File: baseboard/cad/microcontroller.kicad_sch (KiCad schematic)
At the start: 12 parts, among them J16 Conn_01x04_Pin, K1 TQ2-L2-3V3, K2 TQ2-L2-3V3, SW3 SW_DIP_x01, U10 STM32L011F3Ux, U11 DRV8212P, U12 DRV8212P, Y1 830054236

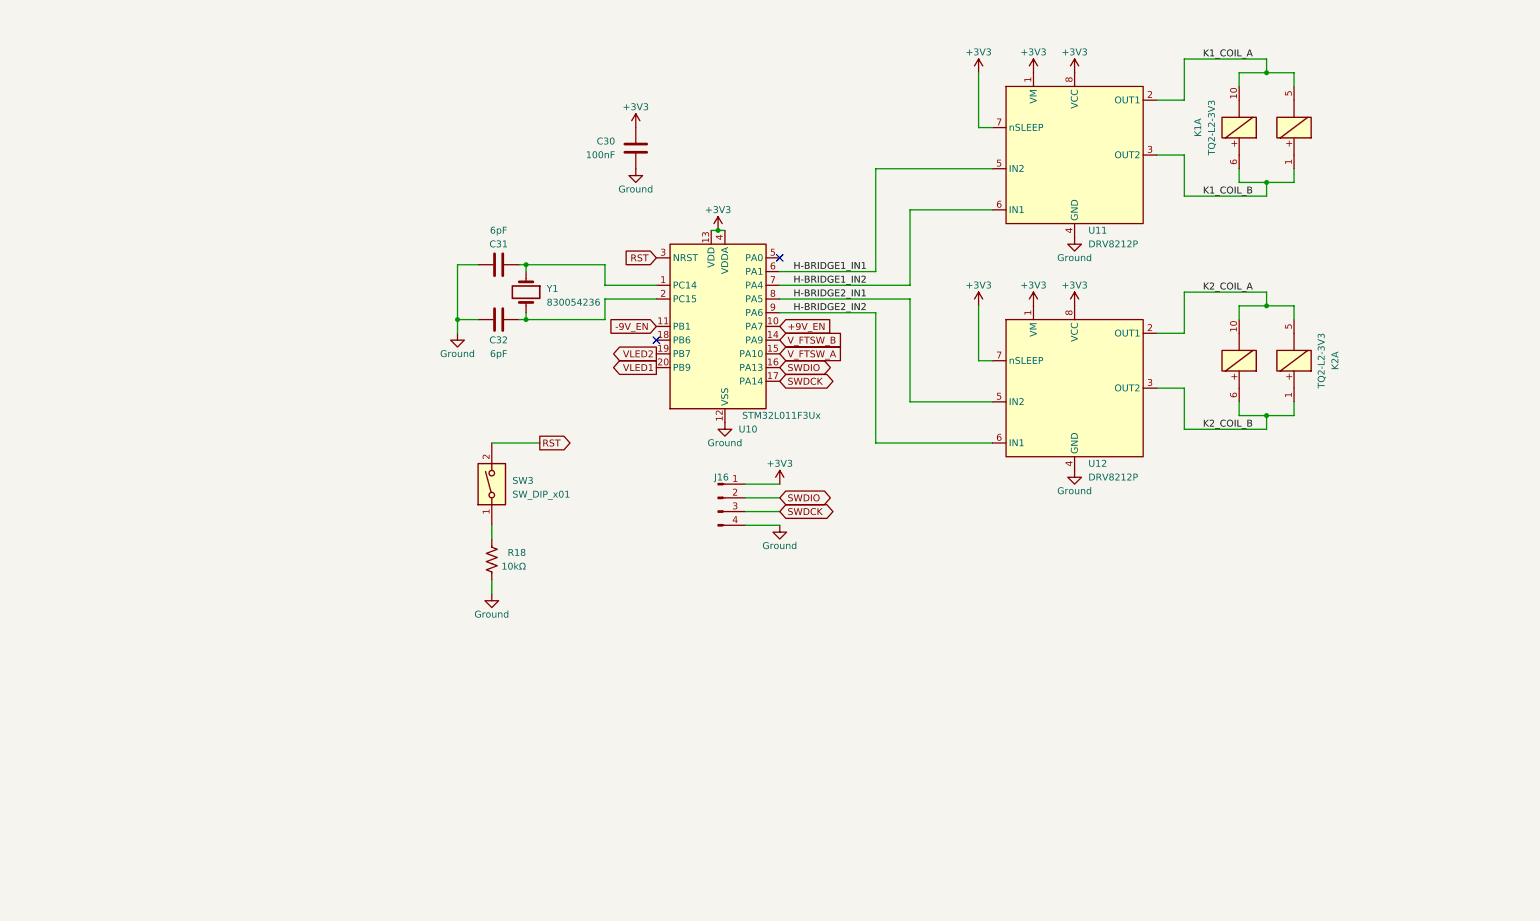
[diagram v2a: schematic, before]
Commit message: swapped micro and started layout
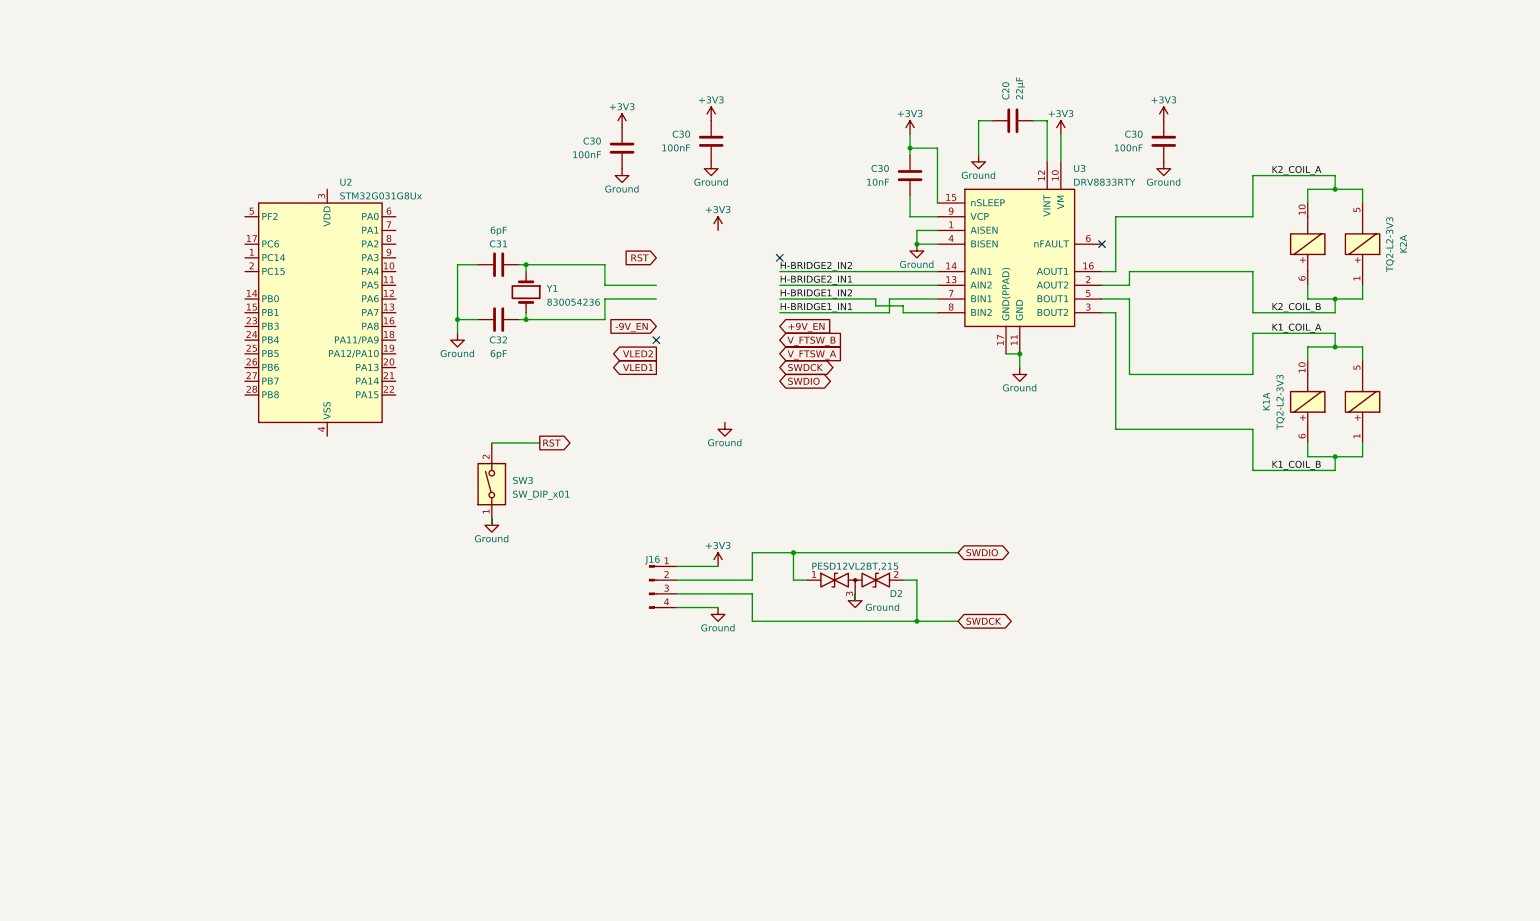
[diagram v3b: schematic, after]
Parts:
- removed R18: 10kΩ, Resistor_SMD:R_0603_1608Metric, symbol Device:R_US
- removed U10: STM32L011F3Ux, Package_DFN_QFN:ST_UFQFPN-20_3x3mm_P0.5mm, symbol MCU_ST_STM32L0:STM32L011F3Ux
- removed U11, U12: DRV8212P, Package_SON:WSON-8-1EP_2x2mm_P0.5mm_EP0.9x1.6mm, symbol Library:DRV8212P
- added C20: 22μF, Capacitor_SMD:C_0805_2012Metric, symbol Device:C
- added C30 (x2): 100nF, Capacitor_SMD:C_1206_3216Metric, symbol Device:C
- added C30: 10nF, Capacitor_SMD:C_1206_3216Metric, symbol Device:C
- added D2: PESD12VL2BT,215, Package_TO_SOT_SMD:SOT-23, symbol Library:PESD12VL2BT,215
- added U2: STM32G031G8Ux, Package_DFN_QFN:QFN-28_4x4mm_P0.5mm, symbol MCU_ST_STM32G0:STM32G031G8Ux
- added U3: DRV8833RTY, Package_DFN_QFN:Texas_S-PWQFN-N16_EP2.1x2.1mm_ThermalVias, symbol Driver_Motor:DRV8833RTY
- J16: footprint (none) -> Connector_PinHeader_2.54mm:PinHeader_1x04_P2.54mm_Vertical
- SW3: footprint (none) -> Button_Switch_SMD:SW_Push_SPST_NO_Alps_SKRK
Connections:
- net +3V3: now also C30.2, C30.2, C30.2, U3.10 (VM), U3.15 (nSLEEP)
- net GND: now also SW3.1, C20.2, C30.1, C30.1, D2.3 (common), U3.1 (AISEN), U3.11 (GND), U3.17 (GND(PPAD)), U3.4 (BISEN)
- net H-BRIDGE1_IN1: now also U3.7 (BIN1)
- net H-BRIDGE1_IN2: now also U3.8 (BIN2)
- net H-BRIDGE2_IN1: now also U3.13 (AIN2)
- net H-BRIDGE2_IN2: now also U3.14 (AIN1)
- net K1_COIL_A: now also U3.5 (BOUT1)
- net K1_COIL_B: now also U3.3 (BOUT2)
- net K2_COIL_A: now also U3.16 (AOUT1)
- net K2_COIL_B: now also U3.2 (AOUT2)
- net SWDCK: now also D2.2 (A2)
- net SWDIO: now also D2.1 (A1)
- new net: C20.1, U3.12 (VINT)
- new net: C30.1, U3.9 (VCP)
- no-connect marks 2 -> 3
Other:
- moved on the sheet: C30, J16

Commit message: picked a third micro for extra pins, updated drd and refdoc.mplstyle
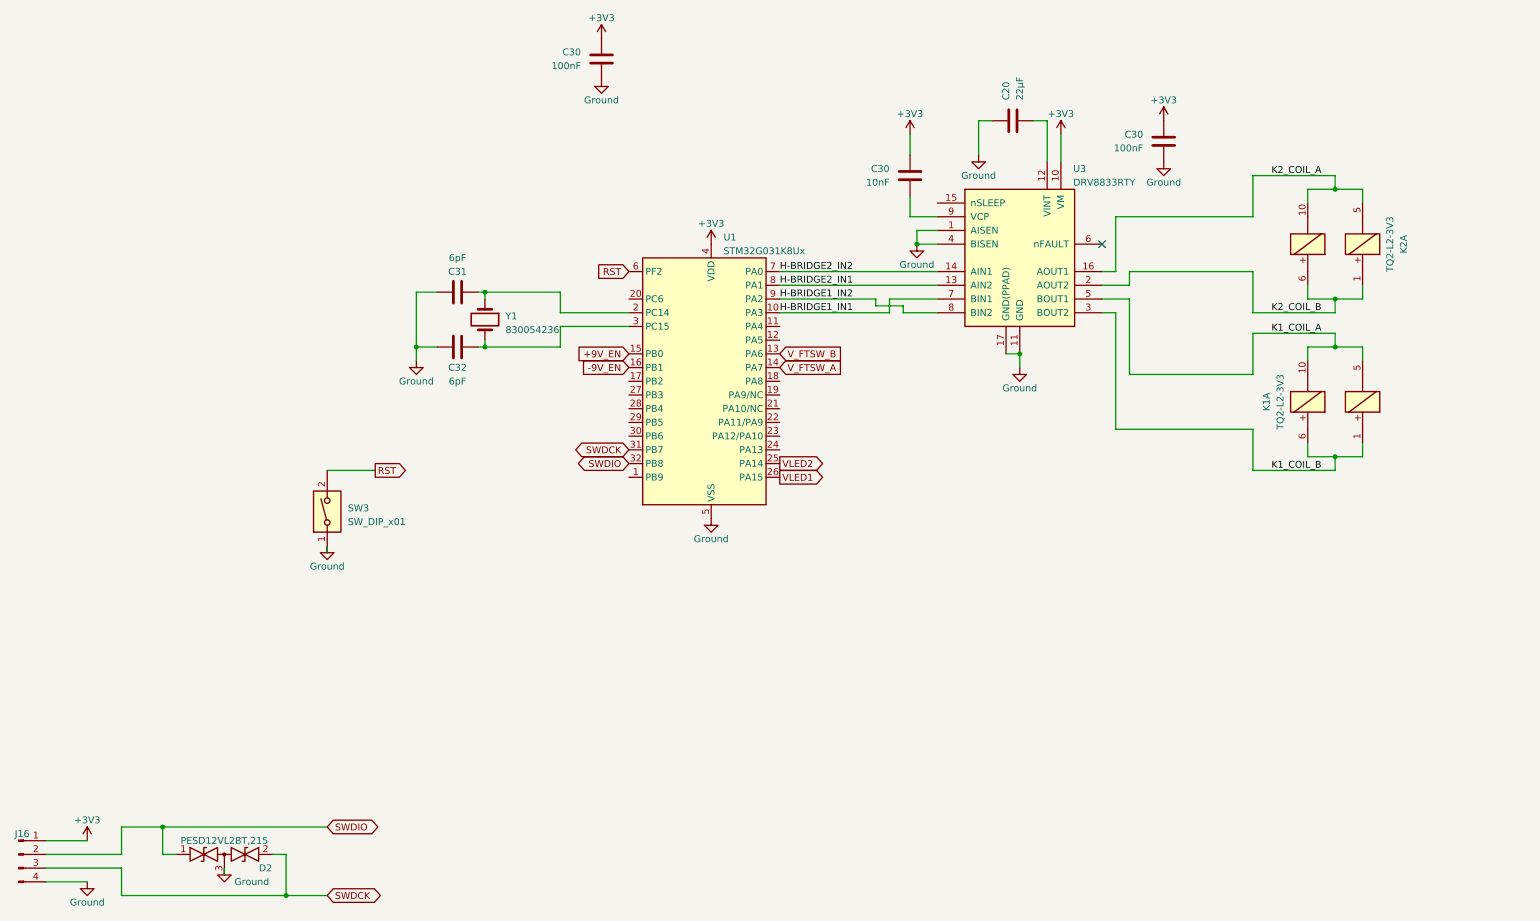
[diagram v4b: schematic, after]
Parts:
- removed C30: 100nF, Capacitor_SMD:C_1206_3216Metric, symbol Device:C
- removed U2: STM32G031G8Ux, Package_DFN_QFN:QFN-28_4x4mm_P0.5mm, symbol MCU_ST_STM32G0:STM32G031G8Ux
- added U1: STM32G031K8Ux, Package_DFN_QFN:QFN-32-1EP_5x5mm_P0.5mm_EP3.45x3.45mm, symbol MCU_ST_STM32G0:STM32G031K8Ux
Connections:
- net +3V3: now also U1.4 (VDD); no longer U3.15 (nSLEEP)
- net +9V_EN: now also U1.15 (PB0)
- net -9V_EN: now also U1.16 (PB1)
- net GND: now also U1.33 (VSS), U1.5 (VSS)
- net H-BRIDGE1_IN1: now also U1.10 (PA3)
- net H-BRIDGE1_IN2: now also U1.9 (PA2)
- net H-BRIDGE2_IN1: now also U1.8 (PA1)
- net H-BRIDGE2_IN2: now also U1.7 (PA0)
- net RST: now also U1.6 (PF2)
- net SWDCK: now also U1.31 (PB7)
- net SWDIO: now also U1.32 (PB8)
- net VLED1: now also U1.26 (PA15)
- net VLED2: now also U1.25 (PA14)
- net V_FTSW_A: now also U1.14 (PA7)
- net V_FTSW_B: now also U1.13 (PA6)
- net at C31.1, Y1.1: now also U1.2 (PC14)
- net at C32.1, Y1.2: now also U1.3 (PC15)
- no-connect marks 3 -> 1
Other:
- moved on the sheet: C30, C31, C32, D2, J16, SW3, Y1

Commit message: placed components and finished new micro hw
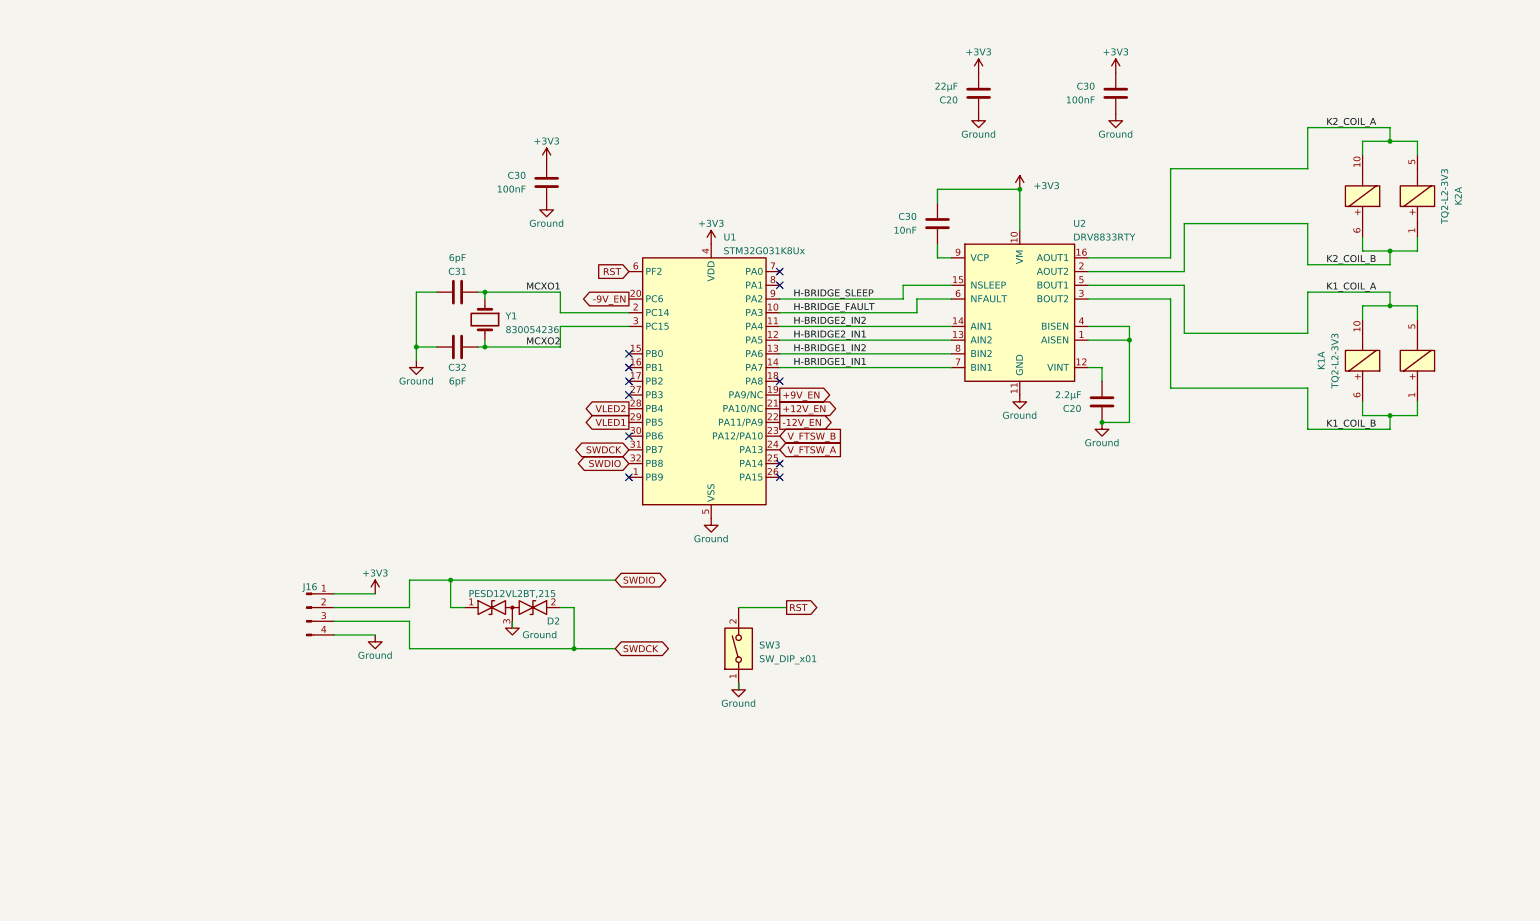
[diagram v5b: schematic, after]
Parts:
- removed C20: 22μF, Capacitor_SMD:C_0805_2012Metric, symbol Device:C
- removed C30: 100nF, Capacitor_SMD:C_1206_3216Metric, symbol Device:C
- removed C30: 10nF, Capacitor_SMD:C_1206_3216Metric, symbol Device:C
- removed U3: DRV8833RTY, Package_DFN_QFN:Texas_S-PWQFN-N16_EP2.1x2.1mm_ThermalVias, symbol Driver_Motor:DRV8833RTY
- added C20: 2.2μF, Capacitor_SMD:C_0805_2012Metric, symbol Device:C
- added C20: 22μF, Capacitor_SMD:C_0805_2012Metric, symbol Device:C
- added C30: 100nF, Capacitor_SMD:C_1206_3216Metric, symbol Device:C
- added C30: 10nF, Capacitor_SMD:C_1206_3216Metric, symbol Device:C
- added U2: DRV8833RTY, Package_DFN_QFN:Texas_S-PWQFN-N16_EP2.1x2.1mm_ThermalVias, symbol Driver_Motor:DRV8833RTY
- U1: footprint Package_DFN_QFN:QFN-32-1EP_5x5mm_P0.5mm_EP3.45x3.45mm -> Package_DFN_QFN:QFN-32-1EP_5x5mm_P0.5mm_EP3.45x3.45mm_ThermalVias
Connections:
- net +3V3: now also C20.1, C30.2, C30.2, U2.10 (VM)
- net +9V_EN: now also U1.19 (PA9/NC); no longer U1.15 (PB0)
- net -9V_EN: now also U1.20 (PC6); no longer U1.16 (PB1)
- net GND: now also C20.2, C20.2, C30.1, U2.1 (AISEN), U2.11 (GND), U2.17 (GND(PPAD)), U2.4 (BISEN)
- net H-BRIDGE1_IN1: now also U1.14 (PA7), U2.7 (BIN1); no longer U1.10 (PA3)
- net H-BRIDGE1_IN2: now also U1.13 (PA6), U2.8 (BIN2); no longer U1.9 (PA2)
- net H-BRIDGE2_IN1: now also U1.12 (PA5), U2.13 (AIN2); no longer U1.8 (PA1)
- net H-BRIDGE2_IN2: now also U1.11 (PA4), U2.14 (AIN1); no longer U1.7 (PA0)
- net K1_COIL_A: now also U2.5 (BOUT1)
- net K1_COIL_B: now also U2.3 (BOUT2)
- net K2_COIL_A: now also U2.16 (AOUT1)
- net K2_COIL_B: now also U2.2 (AOUT2)
- net VLED1: now also U1.29 (PB5); no longer U1.26 (PA15)
- net VLED2: now also U1.28 (PB4); no longer U1.25 (PA14)
- net V_FTSW_A: now also U1.24 (PA13); no longer U1.14 (PA7)
- net V_FTSW_B: now also U1.23 (PA12/PA10); no longer U1.13 (PA6)
- net MCXO1: now reaches C31.1, U1.2 (PC14), Y1.1
- net MCXO2: now reaches C32.1, U1.3 (PC15), Y1.2
- net +12V_EN: now reaches U1.21 (PA10/NC)
- net -12V_EN: now reaches U1.22 (PA11/PA9)
- new net: C20.1, U2.12 (VINT)
- new net: C30.1, U2.9 (VCP)
- new net H-BRIDGE_FAULT: U1.10 (PA3), U2.6 (NFAULT)
- new net H-BRIDGE_SLEEP: U1.9 (PA2), U2.15 (NSLEEP)
- no-connect marks 1 -> 11
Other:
- moved on the sheet: C30, D2, J16, SW3

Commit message: swapped relays for nice analog switch, saved $4
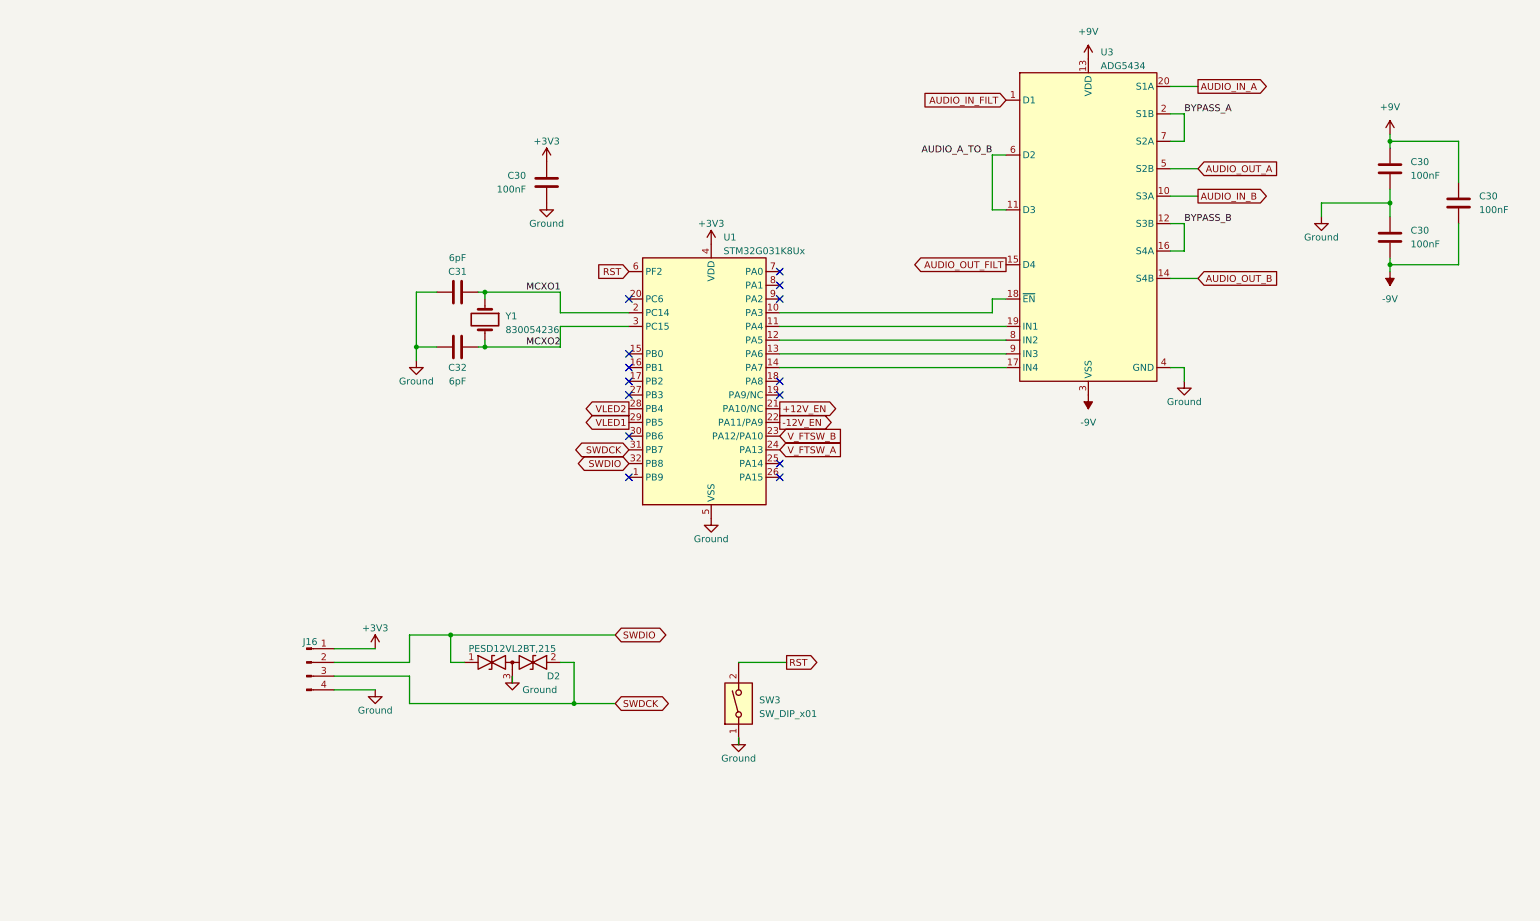
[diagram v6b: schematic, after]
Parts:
- removed C20: 2.2μF, Capacitor_SMD:C_0805_2012Metric, symbol Device:C
- removed C20: 22μF, Capacitor_SMD:C_0805_2012Metric, symbol Device:C
- removed C30: 100nF, Capacitor_SMD:C_1206_3216Metric, symbol Device:C
- removed C30: 10nF, Capacitor_SMD:C_1206_3216Metric, symbol Device:C
- removed K1, K2: TQ2-L2-3V3, Library:Panasonic_TQ2-L2-5V, symbol Library:TQ2-L2-9V
- removed U2: DRV8833RTY, Package_DFN_QFN:Texas_S-PWQFN-N16_EP2.1x2.1mm_ThermalVias, symbol Driver_Motor:DRV8833RTY
- added C30 (x3): 100nF, Capacitor_SMD:C_1206_3216Metric, symbol Device:C
- added U3: ADG5434, Package_CSP:LFCSP-20-1EP_4x4mm_P0.5mm_EP2.6x2.6mm, symbol Library:Analog_Devices_ADG5433
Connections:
- net GND: now also C30.1, C30.2, U3.4 (GND)
- net +9V_EN: no longer names the net of U1.19 (PA9/NC)
- net -9V_EN: no longer names the net of U1.20 (PC6)
- net H-BRIDGE1_IN1: no longer names the net of U1.14 (PA7)
- net H-BRIDGE1_IN1: now also U3.17 (IN4)
- net H-BRIDGE1_IN2: no longer names the net of U1.13 (PA6)
- net H-BRIDGE1_IN2: now also U3.9 (IN3)
- net H-BRIDGE2_IN1: no longer names the net of U1.12 (PA5)
- net H-BRIDGE2_IN1: now also U3.8 (IN2)
- net H-BRIDGE2_IN2: no longer names the net of U1.11 (PA4)
- net H-BRIDGE2_IN2: now also U3.19 (IN1)
- net H-BRIDGE_FAULT: no longer names the net of U1.10 (PA3)
- net H-BRIDGE_FAULT: now also U3.18 (~{EN})
- net H-BRIDGE_SLEEP: no longer names the net of U1.9 (PA2)
- new net +9V: C30.2, C30.2, U3.13 (VDD)
- new net -9V: C30.1, C30.1, U3.21 (VSS), U3.3 (VSS)
- new net AUDIO_A_TO_B: U3.11 (D3), U3.6 (D2)
- new net AUDIO_IN_A: U3.20 (S1A)
- new net AUDIO_IN_B: U3.10 (S3A)
- new net AUDIO_IN_FILT: U3.1 (D1)
- new net AUDIO_OUT_A: U3.5 (S2B)
- new net AUDIO_OUT_B: U3.14 (S4B)
- new net AUDIO_OUT_FILT: U3.15 (D4)
- new net BYPASS_A: U3.2 (S1B), U3.7 (S2A)
- new net BYPASS_B: U3.12 (S3B), U3.16 (S4A)
- no-connect marks 11 -> 14
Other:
- moved on the sheet: D2, J16, SW3
